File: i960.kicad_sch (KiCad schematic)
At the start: 64 parts

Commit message: Reset circuit handled by an AHC138
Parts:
- added C?: (no value), symbol Device:C
- added RN?: (no value), symbol Device:R_Network08
- added U?: (no value), symbol 74xx:74LS138
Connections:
- net +5V: now also C?.1, RN?.1 (common), U?.16 (VCC)
- net GND: now also C?.2, U?.8 (GND)
- net ME_FAIL_IN: now also U?.13 ((AIN4)PD4); no longer U?.20 ((AIN9/MISO_ALT)PE1)
- net i960.~{RESET}: now also U?.6; no longer U?.26 ((AIN13/XDIR2/CCL3-OUT)PF3)
- net ~{READY}: now also U?.14 ((AIN5)PD5); no longer U?.33 ((CLKI/TXD0/CCL0-IN0)PA0)
- net ~{RESET}: now also U?.6 (E3)
- net ~{PIC_BOOTED}: now reaches U?.22 ((AIN11/~{SS}_ALT)PE3)
- net ~{PIC_BOOTED}: now also RN?.3 (R2), U?.2 (A1)
- net at U?.5: now also U?.15 (O0)
- net ~{ME_BOOTED}: now reaches U?.22 ((AIN11/~{SS}_ALT)PE3)
- net ~{ME_BOOTED}: now also RN?.2 (R1), U?.1 (A0)
- new net ~{CHIPSET_BOOTED}: U?.3 (A2)
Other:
- moved on the sheet: U?C

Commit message: Use the Management Engine for the reset controller.
It becomes much easier to work around logic bugs with the CCL. I just
setup PF0 as an output but wire that to CCL3.EVTA (I do this for the
	10MHz signal tests where I routed PA7 as a event source)

So that allows me to control the CCL that way. If that fails then I can
just do polling on boot with no problems.

I also added pullups to make sure that on a reset from the chipset we
will keep the i960 in reset.
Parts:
- removed C?: (no value), symbol Device:C
- removed U?: (no value), symbol 74xx:74LS138
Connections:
- net i960.~{BLAST}: now also U?.15 ((AIN6)PD6)
- net ~{ME_BOOTED}: now also U?.23 ((TOSC1/TXD2/CCL3-IN0)PF0); no longer U?.22 ((AIN11/~{SS}_ALT)PE3)
- net ~{PIC_BOOTED}: now also U?.24 ((TOSC2/RXD2/CCL3-IN1)PF1)
- net ~{READY}: now also U?.19 ((AIN8/MOSI_ALT)PE0); no longer U?.14 ((AIN5)PD5)
- net ~{RESET}: no longer U?.29 (PF6(~{RESET})), U?.29 (PF6(~{RESET}))
- net ~{RESET_INTERMEDIATE}: now reaches U?.5
- net ~{RESET_INTERMEDIATE}: now also RN?.4 (R3), U?.26 ((AIN13/XDIR2/CCL3-OUT)PF3)
- net 5V_~{CHIPSET_BOOTED}: now reaches RN?.5 (R4)
- net 5V_~{CHIPSET_BOOTED}: now also U?.25 ((AIN12/XCK2/CCL3-IN2)PF2)
- new net 5V_~{RESET}: U?.29 (PF6(~{RESET})), U?.29 (PF6(~{RESET}))
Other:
- moved on the sheet: RN?, U?C

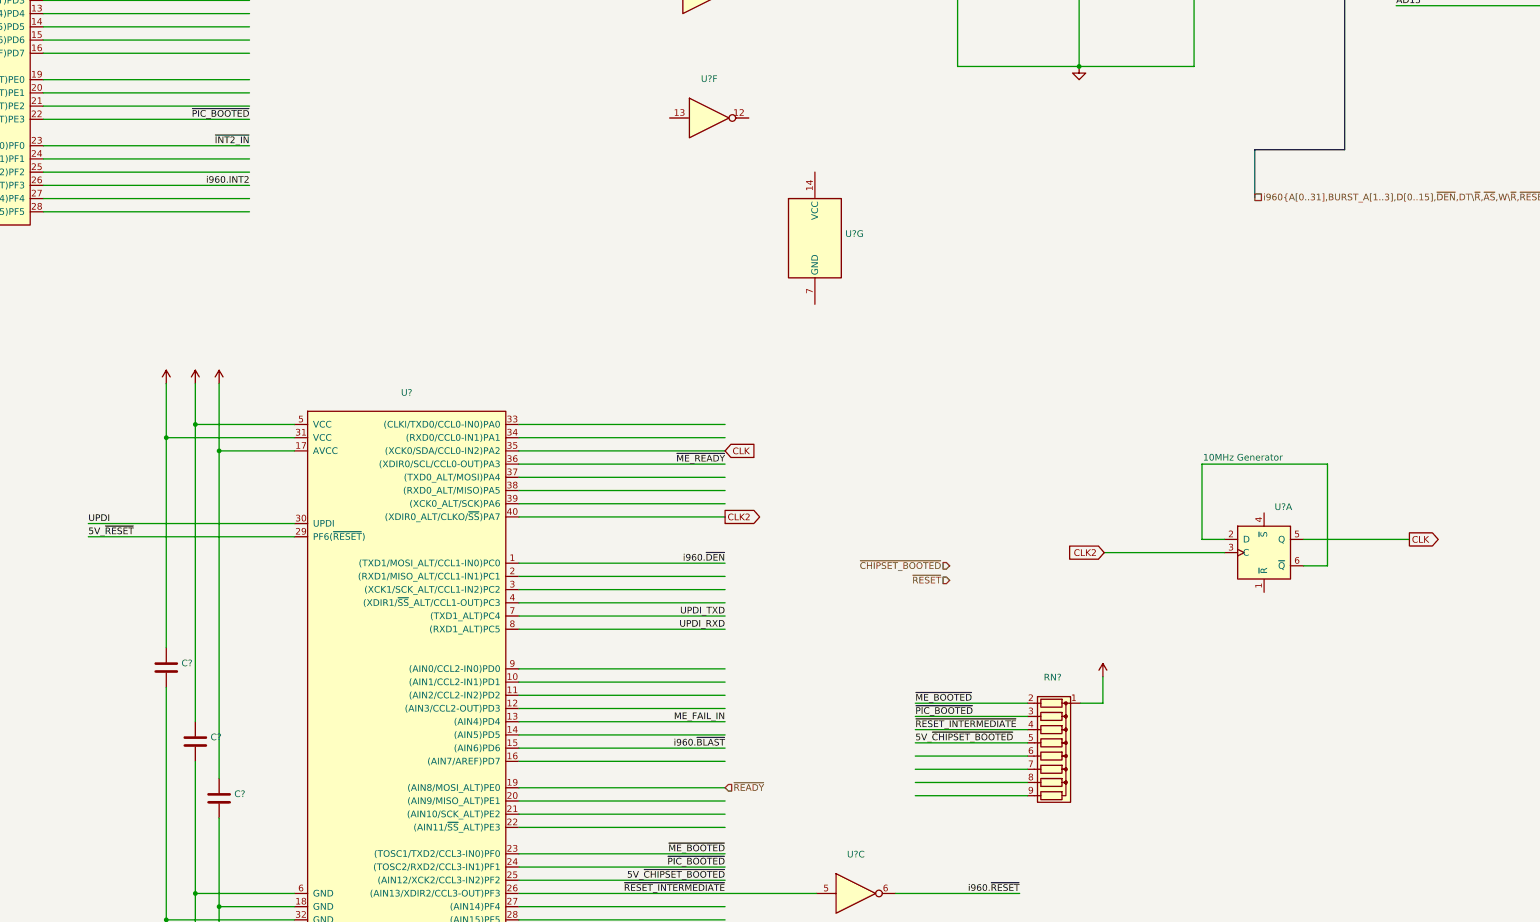
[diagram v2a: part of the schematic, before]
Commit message: Integrate the 10MHz signal generator into the Management Engine
Makes it much easier to control things
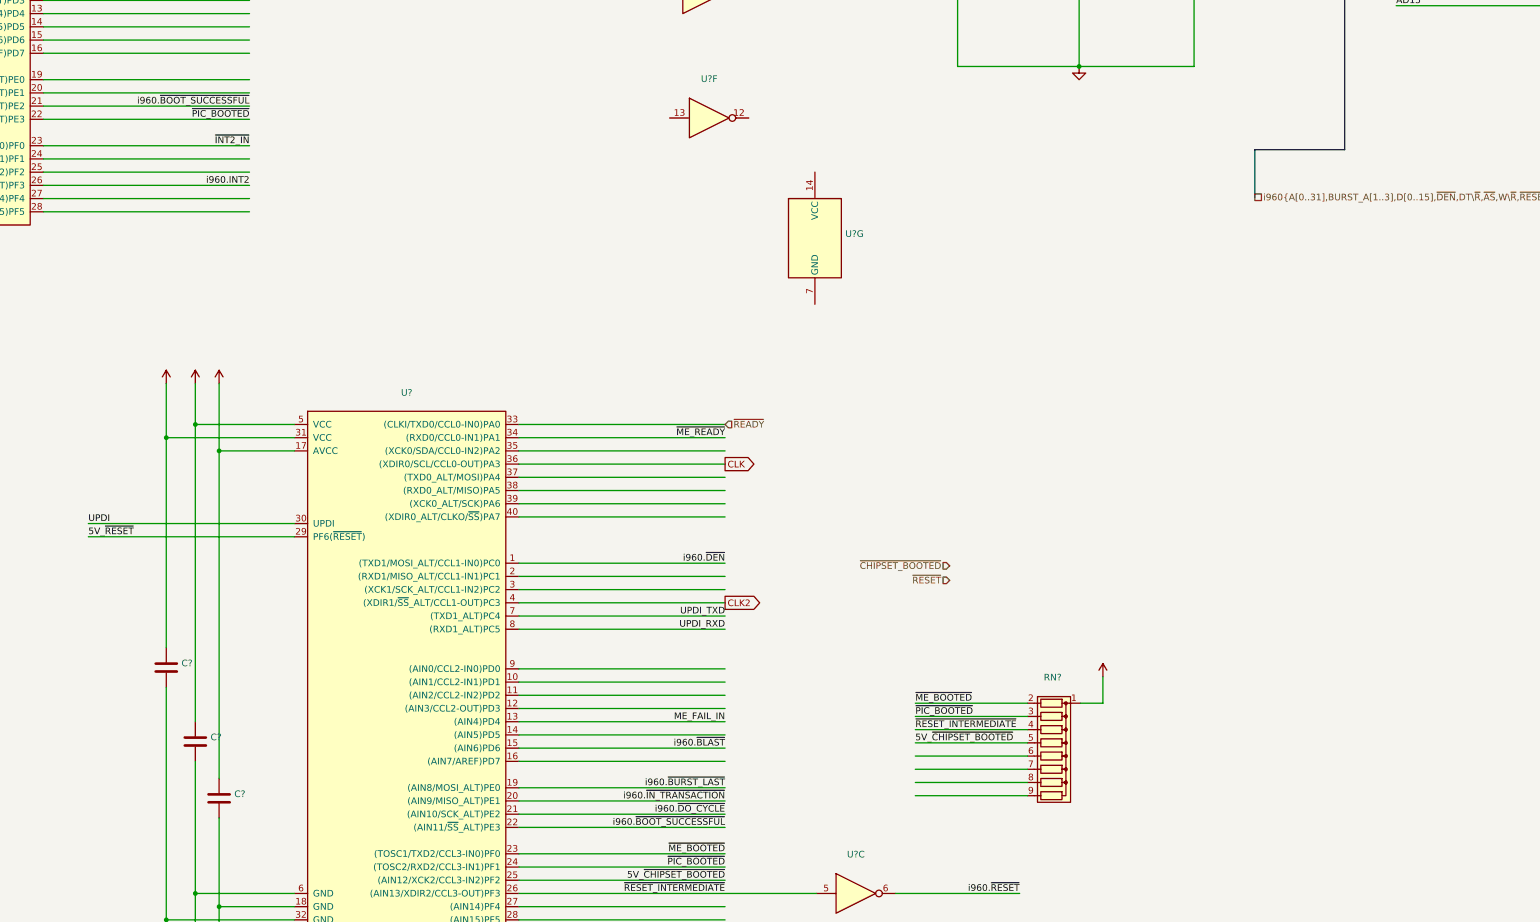
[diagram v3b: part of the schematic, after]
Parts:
- removed U?: (no value), symbol 74xx:74HC74
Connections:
- net CLK: now also U?.36 ((XDIR0/SCL/CCL0-OUT)PA3); no longer U?.35 ((XCK0/SDA/CCL0-IN2)PA2)
- net CLK2: now also U?.4 ((XDIR1/~{SS}_ALT/CCL1-OUT)PC3); no longer U?.40 ((XDIR0_ALT/CLKO/~{SS})PA7)
- net ~{ME_READY}: now also U?.34 ((RXD0/CCL0-IN1)PA1); no longer U?.36 ((XDIR0/SCL/CCL0-OUT)PA3)
- net ~{READY}: now also U?.33 ((CLKI/TXD0/CCL0-IN0)PA0); no longer U?.19 ((AIN8/MOSI_ALT)PE0)
- net i960.~{BOOT_SUCCESSFUL}: now reaches U?.21 ((AIN10/SCK_ALT)PE2)
- net i960.~{BOOT_SUCCESSFUL}: now also U?.22 ((AIN11/~{SS}_ALT)PE3)
- net i960.~{IN_TRANSACTION}: now reaches U?.20 ((AIN9/MISO_ALT)PE1)
- net i960.~{DO_CYCLE}: now reaches U?.21 ((AIN10/SCK_ALT)PE2)
- new net i960.~{BURST_LAST}: U?.19 ((AIN8/MOSI_ALT)PE0)
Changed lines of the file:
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@@
-    (stroke (width 0) (type default) (color 0 0 0 0))
-  )
-  (wire (pts (xy 476.758 297.18) (xy 452.628 297.18))
     (stroke (width 0) (type default) (color 0 0 0 0))
   )
@@
     (stroke (width 0) (type default) (color 0 0 0 0))
   )
-  (wire (pts (xy 472.186 316.738) (xy 476.758 316.738))
-    (stroke (width 0) (type default) (color 0 0 0 0))
-  )
   (bus (pts (xy 480.06 181.356) (xy 480.06 183.896))
     (stroke (width 0) (type default) (color 0 0 0 0))
@@
     (stroke (width 0) (type default) (color 0 0 0 0))
   )
-  (wire (pts (xy 472.186 311.658) (xy 492.506 311.658))
-    (stroke (width 0) (type default) (color 0 0 0 0))
-  )
   (wire (pts (xy 65.786 111.252) (xy 63.246 111.252))
     (stroke (width 0) (type default) (color 0 0 0 0))
@@
     (stroke (width 0) (type default) (color 0 0 0 0))
   )
-  (wire (pts (xy 452.628 297.18) (xy 452.628 311.658))
-    (stroke (width 0) (type default) (color 0 0 0 0))
-  )
   (wire (pts (xy 186.69 153.416) (xy 167.64 153.416))
     (stroke (width 0) (type default) (color 0 0 0 0))
@@
     (stroke (width 0) (type default) (color 0 0 0 0))
   )
-  (wire (pts (xy 476.758 316.738) (xy 476.758 297.18))
-    (stroke (width 0) (type default) (color 0 0 0 0))
-  )
   (wire (pts (xy 121.412 371.348) (xy 121.412 368.554))
     (stroke (width 0) (type default) (color 0 0 0 0))
@@
   )
   (wire (pts (xy 380.492 191.516) (xy 416.306 191.516))
-    (stroke (width 0) (type default) (color 0 0 0 0))
-  )
-  (wire (pts (xy 452.628 311.658) (xy 456.946 311.658))
-    (stroke (width 0) (type default) (color 0 0 0 0))
-  )
-  (wire (pts (xy 433.832 314.198) (xy 456.946 314.198))
     (stroke (width 0) (type default) (color 0 0 0 0))
   )
@@
     (effects (font (size 1.27 1.27)) (justify right bottom))
   )
+  (label "i960.~{BOOT_SUCCESSFUL}" (at 269.494 228.346 180)
+    (effects (font (size 1.27 1.27)) (justify right bottom))
+  )
   (label "i960.A23" (at 515.874 77.724 0)
     (effects (font (size 1.27 1.27)) (justify left bottom))
@@
     (effects (font (size 1.27 1.27)) (justify right bottom))
   )
+  (label "i960.~{IN_TRANSACTION}" (at 360.934 361.95 180)
+    (effects (font (size 1.27 1.27)) (justify right bottom))
+  )
   (label "i960.~{BLAST}" (at 570.738 191.262 180)
     (effects (font (size 1.27 1.27)) (justify right bottom))
@@
     (effects (font (size 1.27 1.27)) (justify left bottom))
   )
-  (label "~{ME_READY}" (at 360.934 297.18 180)
+  (label "~{ME_READY}" (at 360.934 292.1 180)
     (effects (font (size 1.27 1.27)) (justify right bottom))
   )
@@
     (effects (font (size 1.27 1.27)) (justify right bottom))
   )
+  (label "i960.~{BURST_LAST}" (at 360.934 359.41 180)
+    (effects (font (size 1.27 1.27)) (justify right bottom))
+  )
   (label "i960.~{BE0}" (at 36.068 93.472 0)
     (effects (font (size 1.27 1.27)) (justify left bottom))
@@
     (effects (font (size 1.27 1.27)) (justify left bottom))
   )
+  (label "i960.~{DO_CYCLE}" (at 360.934 364.49 180)
+    (effects (font (size 1.27 1.27)) (justify right bottom))
+  )
   (label "~{FAIL_SIG}" (at 144.272 100.838 0)
     (effects (font (size 1.27 1.27)) (justify left bottom))
@@
   )
   (label "~{FAIL_SIG}" (at 101.6 101.092 180)
+    (effects (font (size 1.27 1.27)) (justify right bottom))
+  )
+  (label "i960.~{BOOT_SUCCESSFUL}" (at 360.934 367.03 180)
     (effects (font (size 1.27 1.27)) (justify right bottom))
   )
@@
     )
   )
-  (global_label "CLK" (shape output) (at 492.506 311.658 0) (fields_autoplaced)
+  (global_label "CLK" (shape output) (at 360.934 297.18 0) (fields_autoplaced)
     (effects (font (size 1.27 1.27)) (justify left))
-    (property "Intersheet References" "${INTERSHEET_REFS}" (id 0) (at 498.3983 311.5786 0)
+    (property "Intersheet References" "${INTERSHEET_REFS}" (id 0) (at 366.8263 297.1006 0)
       (effects (font (size 1.27 1.27)) (justify left) hide)
     )
   )
-  (global_label "CLK" (shape input) (at 360.934 294.64 0) (fields_autoplaced)
+  (global_label "CLK2" (shape output) (at 360.934 323.85 0) (fields_autoplaced)
     (effects (font (size 1.27 1.27)) (justify left))
-    (property "Intersheet References" "${INTERSHEET_REFS}" (id 0) (at 366.8263 294.7194 0)
-      (effects (font (size 1.27 1.27)) (justify left) hide)
-    )
-  )
-  (global_label "CLK2" (shape input) (at 433.832 314.198 180) (fields_autoplaced)
-    (effects (font (size 1.27 1.27)) (justify right))
-    (property "Intersheet References" "${INTERSHEET_REFS}" (id 0) (at 426.7302 314.1186 0)
-      (effects (font (size 1.27 1.27)) (justify right) hide)
-    )
-  )
-  (global_label "CLK2" (shape output) (at 360.934 307.34 0) (fields_autoplaced)
-    (effects (font (size 1.27 1.27)) (justify left))
-    (property "Intersheet References" "${INTERSHEET_REFS}" (id 0) (at 368.0358 307.2606 0)
+    (property "Intersheet References" "${INTERSHEET_REFS}" (id 0) (at 368.0358 323.7706 0)
       (effects (font (size 1.27 1.27)) (justify left) hide)
     )
@@
     (effects (font (size 1.27 1.27)) (justify right))
   )
-  (hierarchical_label "~{READY}" (shape input) (at 360.934 359.41 0)
+  (hierarchical_label "~{READY}" (shape input) (at 360.934 289.56 0)
     (effects (font (size 1.27 1.27)) (justify left))
   )
@@
     (pin "9")
   )
-  (symbol (lib_id "74xx:74HC74") (at 464.566 314.198 0) (unit 1)
-    (in_bom yes) (on_board yes)
-    (property "Reference" "U?" (id 0) (at 466.5854 305.4182 0)
-      (effects (font (size 1.27 1.27)) (justify left))
-    )
-    (property "Value" "" (id 1) (at 466.5854 307.9551 0)
-      (effects (font (size 1.27 1.27)) (justify left))
-    )
-    (property "Footprint" "" (id 2) (at 464.566 314.198 0)
-      (effects (font (size 1.27 1.27)) hide)
-    )
-    (property "Datasheet" "74xx/74hc_hct74.pdf" (id 3) (at 464.566 314.198 0)
-      (effects (font (size 1.27 1.27)) hide)
-    )
-    (property "Function" "10MHz Generator" (id 4) (at 460.502 295.91 0))
-    (pin "1")
-    (pin "2")
-    (pin "3")
-    (pin "4")
-    (pin "5")
-    (pin "6")
-    (pin "10")
-    (pin "11")
-    (pin "12")
-    (pin "13")
-    (pin "8")
-    (pin "9")
-    (pin "14")
-    (pin "7")
-  )
   (symbol (lib_id "74xx:74AHC04") (at 386.08 379.73 0) (unit 3)

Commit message: Put the external ready hardware on a breakout connector
If I run into problems or bugs, we can connect a small handler board
onto the header and override the issue really quickly. If you don't plug
in the connector then no problem we will detect that.

I have it routed through the CCL in a very trivial manner. The nice
thing is that regardless of where we do the ready signal computation we
will always use CCL2.IN0 for ~{ME_READY}
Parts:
- removed RN?: (no value), symbol Device:R_Network08
- removed U? (x7): (no value), symbol 74xx:74AHC04
- removed U? (x2): (no value), symbol 74xx:74HC74
- removed U? (x5): (no value), symbol 74xx:74HC00
- added C?: (no value), symbol Device:C
- added J?: (no value), symbol Connector_Generic:Conn_01x08
- added RN?: (no value), symbol Device:R_Network12
- added U? (x7): (no value), symbol 74xx:74AHC04
- added U?: (no value), symbol 74xx:74HC244
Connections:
- net +5V: now also C?.1, C?.1, J?.2 (Pin_2), RN?.1 (common), U?.14 (VCC), U?.20 (VCC)
- net 5V_~{CHIPSET_BOOTED}: now also RN?.5 (R4), U?.18 (1Y0)
- net 5V_~{RESET}: now also RN?.6 (R5), U?.16 (1Y1); no longer U?.29 (PF6(~{RESET}))
- net CLK: now also J?.3 (Pin_3)
- net CLK2: now also U?.40 ((XDIR0_ALT/CLKO/~{SS})PA7); no longer U?.4 ((XDIR1/~{SS}_ALT/CCL1-OUT)PC3)
- net GND: now also C?.2, C?.2, J?.1 (Pin_1), U?.1 (1OE), U?.10 (GND), U?.19 (2OE), U?.7 (GND)
- net ME_FAIL_IN: now also U?.3 ((XCK1/SCK_ALT/CCL1-IN2)PC2); no longer U?.13 ((AIN4)PD4)
- net i960.~{BLAST}: now also U?.2 ((RXD1/MISO_ALT/CCL1-IN1)PC1); no longer U?.15 ((AIN6)PD6)
- net i960.~{INT0}: now also RN?.8 (R7), U?.8
- net i960.~{INT3}: now also RN?.9 (R8), U?.6
- net i960.~{RESET}: now also U?.4
- net ~{CHIPSET_BOOTED}: now also U?.2 (1A0)
- net ~{INT0_IN}: now also U?.12 (1Y3)
- net ~{INT1_IN}: now also U?.3 (2Y0)
- net ~{INT2_IN}: now also U?.5 (2Y1)
- net ~{INT3_IN}: now also U?.7 (2Y2)
- net ~{ME_BOOTED}: now also RN?.2 (R1)
- net ~{ME_READY}: now also U?.9 ((AIN0/CCL2-IN0)PD0), J?.4 (Pin_4), RN?.13 (R12); no longer U?.34 ((RXD0/CCL0-IN1)PA1)
- net ~{PIC_BOOTED}: now also RN?.3 (R2)
- net ~{READY960}: now also U?.2
- net ~{READY}: now also U?.6 (1A2); no longer U?.33 ((CLKI/TXD0/CCL0-IN0)PA0)
- net ~{RESET_INTERMEDIATE}: now also RN?.4 (R3), U?.3
- net ~{RESET}: now also U?.4 (1A1)
- net at U?.36 ((XDIR0/SCL/CCL0-OUT)PA3): now also U?.5
- net at U?.4 ((XDIR1/~{SS}_ALT/CCL1-OUT)PC3): now also U?.9
- net ~{EXT_READY}: now reaches U?.10 ((AIN1/CCL2-IN1)PD1)
- net ~{EXT_READY}: now also J?.5 (Pin_5), RN?.12 (R11)
- net at U?.12 ((AIN3/CCL2-OUT)PD3): now also U?.1
- net ~{RUN_PIC}: now reaches U?.27 ((AIN14)PF4)
- net ~{RUN_PIC}: now also RN?.7 (R6), U?.11
- new net: U?.10, U?.29 (PF6(~{RESET}))
- new net 5V_~{READY}: U?.14 (1Y2), U?.33 ((CLKI/TXD0/CCL0-IN0)PA0)
- new net 5V_~{REQUEST_HOLD}: RN?.11 (R10), U?.9 (2Y3)
- new net ~{EXT_READY_INSTALLED}: J?.6 (Pin_6), RN?.10 (R9)
- new net ~{INTR0}: U?.8 (1A3)
- new net ~{INTR1}: U?.17 (2A0)
- new net ~{INTR2}: U?.15 (2A1)
- new net ~{INTR3}: U?.13 (2A2)
- new net ~{REQUEST_HOLD}: U?.11 (2A3)
- no-connect marks 2 -> 1
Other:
- note added: "If the management engine is down the PIC should also be down as well! It should not come out of reset until the management engine says so!"

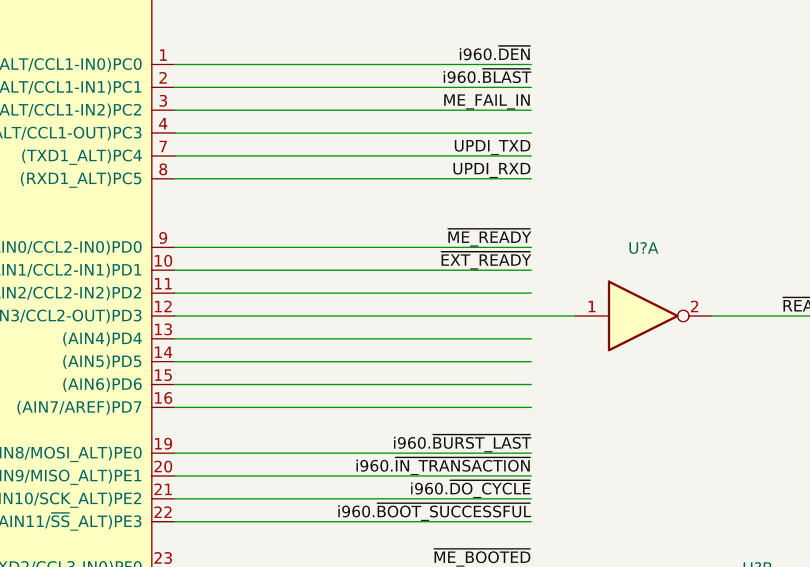
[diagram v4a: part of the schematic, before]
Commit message: Fix a screwup for labels
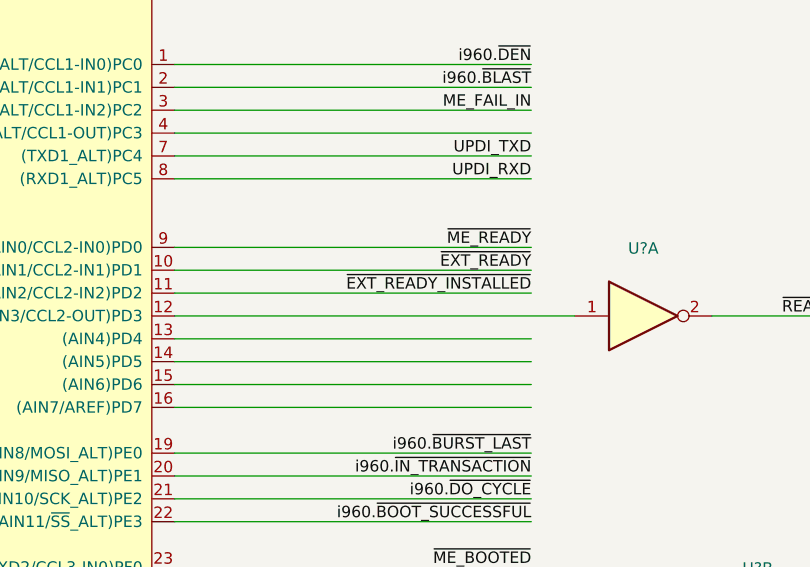
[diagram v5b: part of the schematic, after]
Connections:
- net ~{EXT_READY_INSTALLED}: now also U?.11 ((AIN2/CCL2-IN2)PD2)
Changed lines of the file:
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@@
     (effects (font (size 1.27 1.27)) (justify left bottom))
+  )
+  (label "~{EXT_READY_INSTALLED}" (at 360.934 341.63 180)
+    (effects (font (size 1.27 1.27)) (justify right bottom))
   )
   (label "AD6" (at 442.976 117.094 0)
